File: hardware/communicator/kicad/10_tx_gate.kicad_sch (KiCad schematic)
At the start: 6 parts, among them U24 SN74LVC2G125DCUR, U25 SN74LVC2G125DCUR

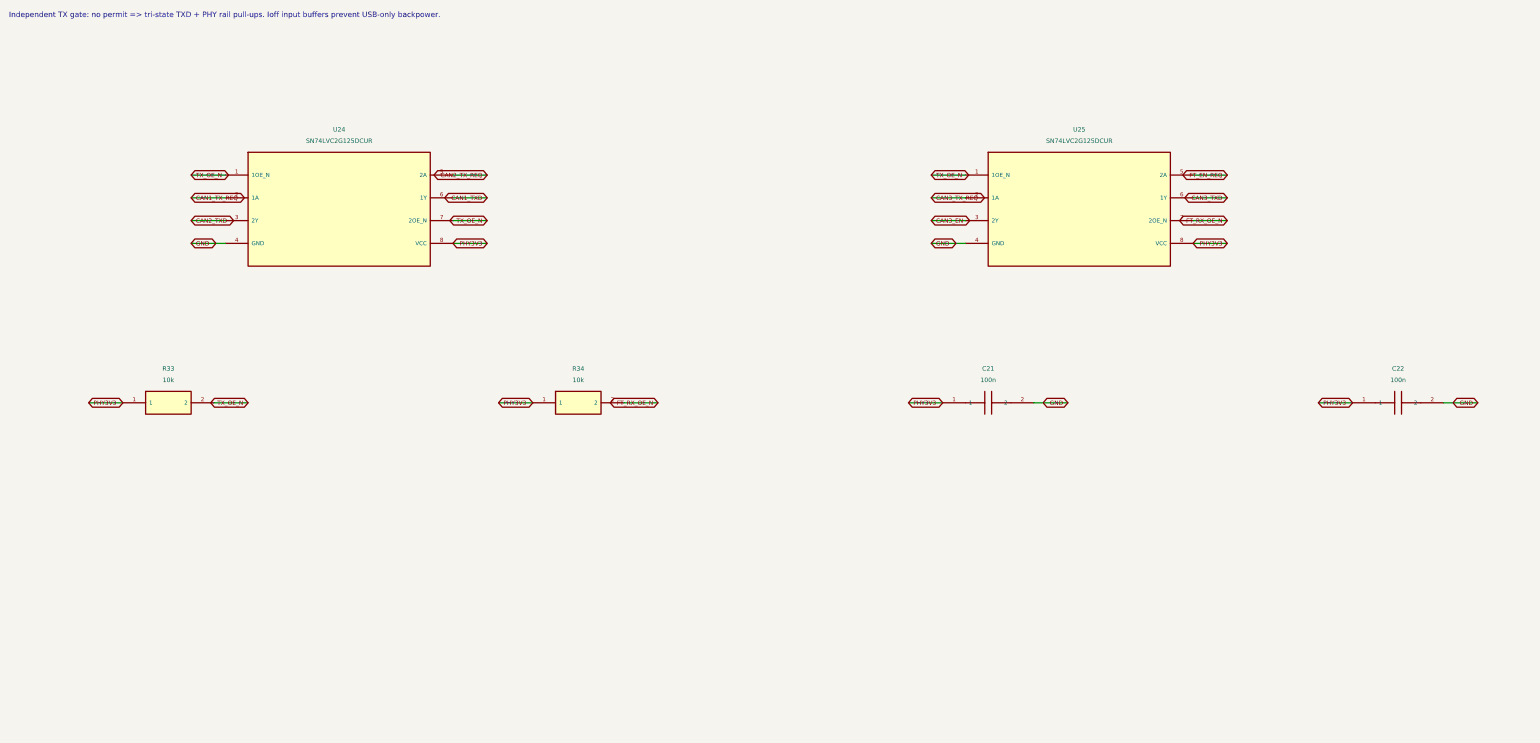
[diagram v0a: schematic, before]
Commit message: feat: add R1 detailed hardware and navigation protocol review candidate
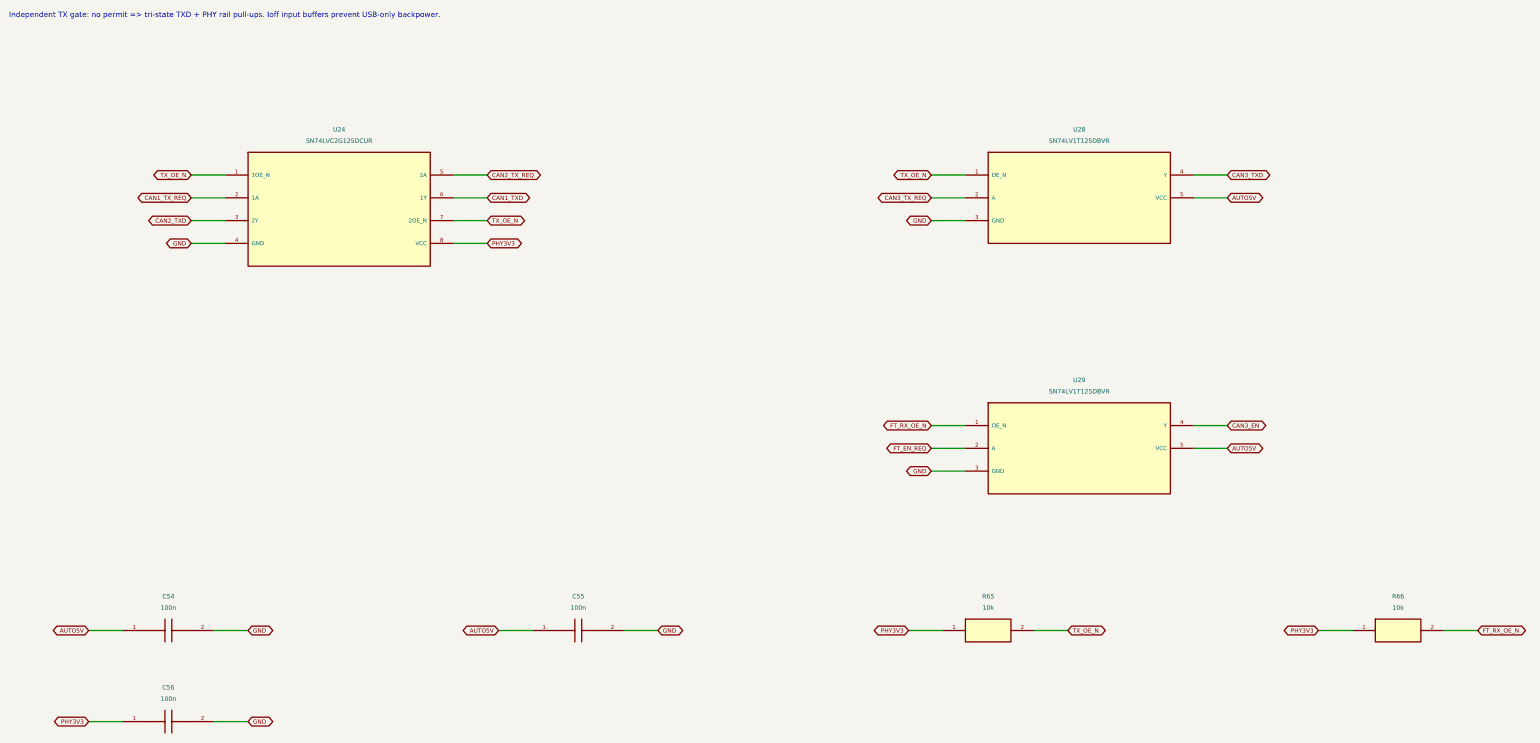
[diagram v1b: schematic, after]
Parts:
- removed C21: 100n, CANView:Capacitor_SMD__C_0402_1005Metric, symbol CANView:CANView_communicator_C21
- removed C22: 100n, CANView:Capacitor_SMD__C_0402_1005Metric, symbol CANView:CANView_communicator_C22
- removed R33: 10k, CANView:Resistor_SMD__R_0402_1005Metric, symbol CANView:CANView_communicator_R33
- removed R34: 10k, CANView:Resistor_SMD__R_0402_1005Metric, symbol CANView:CANView_communicator_R34
- removed U25: SN74LVC2G125DCUR, CANView:Package_SO__VSSOP-8_2.3x2mm_P0.5mm, symbol CANView:CANView_communicator_U25
- added C54: 100n, CANView:Capacitor_SMD__C_0402_1005Metric, symbol CANView:CANView_communicator_C54
- added C55: 100n, CANView:Capacitor_SMD__C_0402_1005Metric, symbol CANView:CANView_communicator_C55
- added C56: 100n, CANView:Capacitor_SMD__C_0402_1005Metric, symbol CANView:CANView_communicator_C56
- added R65: 10k, CANView:Resistor_SMD__R_0402_1005Metric, symbol CANView:CANView_communicator_R65
- added R66: 10k, CANView:Resistor_SMD__R_0402_1005Metric, symbol CANView:CANView_communicator_R66
- added U28: SN74LV1T125DBVR, CANView:Package_TO_SOT_SMD__SOT-23-5, symbol CANView:CANView_communicator_U28
- added U29: SN74LV1T125DBVR, CANView:Package_TO_SOT_SMD__SOT-23-5, symbol CANView:CANView_communicator_U29
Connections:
- net CAN3_EN: now also U29.4 (Y)
- net CAN3_TXD: now also U28.4 (Y)
- net CAN3_TX_REQ: now also U28.2 (A)
- net FT_EN_REQ: now also U29.2 (A)
- net FT_RX_OE_N: now also R66.2, U29.1 (OE_N)
- net GND: now also C54.2, C55.2, C56.2, U28.3 (GND), U29.3 (GND)
- net PHY3V3: now also C56.1, R65.1, R66.1
- net TX_OE_N: now also R65.2, U28.1 (OE_N)
- new net AUTO5V: C54.1, C55.1, U28.5 (VCC), U29.5 (VCC)

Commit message: fix: close hardware rail-fault paths and sensor contract gaps
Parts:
- removed C54: 100n, CANView:Capacitor_SMD__C_0402_1005Metric, symbol CANView:CANView_communicator_C54
- removed C55: 100n, CANView:Capacitor_SMD__C_0402_1005Metric, symbol CANView:CANView_communicator_C55
- removed R65: 10k, CANView:Resistor_SMD__R_0402_1005Metric, symbol CANView:CANView_communicator_R65
- added C57: 100n, CANView:Capacitor_SMD__C_0402_1005Metric, symbol CANView:CANView_communicator_C57
- added C58: 100n, CANView:Capacitor_SMD__C_0402_1005Metric, symbol CANView:CANView_communicator_C58
- added R67: 1k, CANView:Resistor_SMD__R_0402_1005Metric, symbol CANView:CANView_communicator_R67
- added R68: 10k, CANView:Resistor_SMD__R_0402_1005Metric, symbol CANView:CANView_communicator_R68
- added R69: 10k, CANView:Resistor_SMD__R_0402_1005Metric, symbol CANView:CANView_communicator_R69
- R66: value 10k -> 1k; MPN GEN-R-0402-10k-1% -> GEN-R-0402-1k-1%
- U28, U29: value SN74LV1T125DBVR -> SN74AHCT1G126-Q1; MPN SN74LV1T125DBVR -> CAHCT1G126DBVRQ1; Source sn74lv1t125:pp3,5-6; input tolerance independent of supply,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 -> sn74ahct1g126-q1:pp3-5,8,13; active-high OE with pulldown; 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; Specification 3.3V input translated to MAX3055 own5V rail; do not claim g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 -> 3..5.5V supply; TTL VIH2V at5V; active-high permit. OE LOW 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
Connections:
- net AUTO5V: now also C56.1, C57.1
- net FT_RX_OE_N: now also R69.2; no longer R66.2, U29.1 (OE_N)
- net GND: now also R66.2, C57.2, C58.2, R67.2
- net PHY3V3: now also C58.1, R68.1, R69.1; no longer C56.1, R66.1
- net TX_OE_N: now also R68.2; no longer U28.1 (OE_N)
- new net RX_ALLOWED: R67.1, U29.1 (OE)
- new net TX_PERMIT: R66.1, U28.1 (OE)
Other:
- moved on the sheet: C56, R66
